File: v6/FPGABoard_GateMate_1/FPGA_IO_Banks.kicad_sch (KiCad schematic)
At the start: 29 parts, among them U1 CCGM1A1, Y1 AMJMAFB-100.0000T

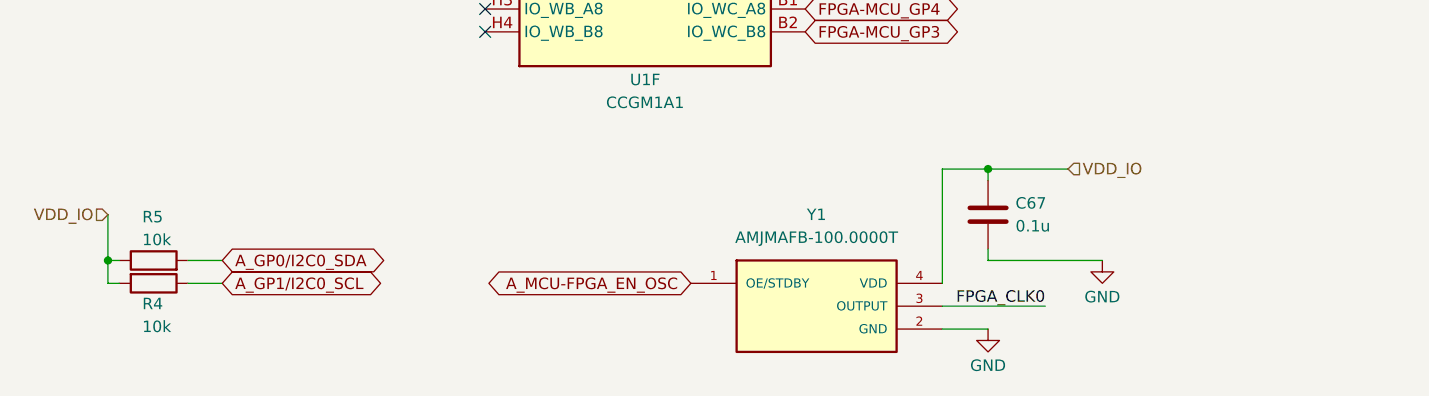
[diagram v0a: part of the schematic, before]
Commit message: Add comments for GateMAte board
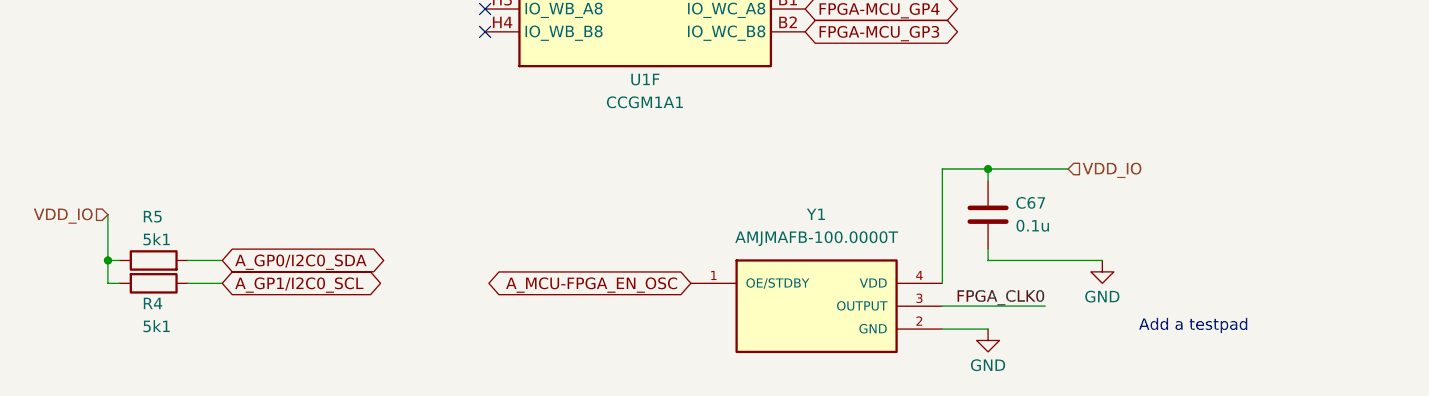
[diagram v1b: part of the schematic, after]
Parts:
- R4, R5: value 10k -> 5k1
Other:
- note added: "Add a testpad"
